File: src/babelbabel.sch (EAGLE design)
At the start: 86 parts, among them CON1 CON-4P-TABS-JST_GH-RA, CON10 CON-6P-SM06B, CON11 PINHEAD_1X04-2.54, CON12 PINHEAD_1X06-2.54, CON15 PINHEAD_1X04-2.54, CON16 CON-4P-TABS-JST_GH-RA, CON2 PINHEAD_1X04-2.54, CON3 PINHEAD_1X04-2.54, CON4 USB-AA-PTH, CON5 CON-4P-TABS-JST_GH-RA, CON6 CON-4P-TABS-JST_GH-RA, CON7 USB-1, IC1 NS5B1G385, IC13 STM32F103CBT7, IC14 74LVC2T45, IC15 74LVC2T45, IC16 74LVC2T45, IC17 74LVC2T45, IC2 NS5B1G385, IC3 AP2127-3.3, IC9 FE1.1S, J1 CONNECTION-SMD, J2 CONNECTION-SMD, Q7 8MHz, Q8 12MHz, Q9 NTZD3152PT1G

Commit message: Revert "source files consistency fix"
This reverts commit 015ba0159d9c48fa3345c98b8ff1ca9c9c6bfb7d.
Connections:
- new net ITDI: IC15.2A
- new net ITDO: IC16.1A
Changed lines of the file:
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@@
 </ports>
 <variantdefs>
-<variantdef name="48_pin_MCU"/>
-<variantdef name="64_pin_MCU"/>
+<variantdef name="A"/>
+<variantdef name="basic"/>
 </variantdefs>
 <parts>
 <part name="IC1" library="stm32" library_urn="urn:adsk.eagle:library:2473361" deviceset="STM32F373CBT6" device="-LQFP48" package3d_urn="urn:adsk.eagle:package:2473350/4">
-<variant name="64_pin_MCU" populate="no"/>
+<variant name="basic" populate="no"/>
 </part>
 <part name="GND1" library="supply_symbols" library_urn="urn:adsk.eagle:library:5017758" deviceset="GND" device="" value="GND"/>
@@
 <part name="P+6" library="supply_symbols" library_urn="urn:adsk.eagle:library:5017758" deviceset="3.3V" device=""/>
 <part name="GND4" library="supply_symbols" library_urn="urn:adsk.eagle:library:5017758" deviceset="GND" device="" value="GND"/>
-<part name="IC8" library="misc" library_urn="urn:adsk.eagle:library:5347860" deviceset="TPD3S014DBVR" device="-SOT23-6" package3d_urn="urn:adsk.eagle:package:1040217/3"/>
+<part name="IC8" library="misc" library_urn="urn:adsk.eagle:library:5347860" deviceset="TPD3S014DBVR" device="-SOT23-6" package3d_urn="urn:adsk.eagle:package:1040217/3">
+<variant name="A" populate="no"/>
+</part>
 <part name="+P4" library="supply_symbols" library_urn="urn:adsk.eagle:library:13097679" deviceset="5V" device=""/>
 <part name="C84" library="rc" library_urn="urn:adsk.eagle:library:2539423" deviceset="C" device="-0402" package3d_urn="urn:adsk.eagle:package:2539461/2" value="0.1uF">
@@
 <part name="IC2" library="stm32" library_urn="urn:adsk.eagle:library:2473361" deviceset="STM32F373RCT6" device="" package3d_urn="urn:adsk.eagle:package:2473349/4">
 <attribute name="DIGIKEY#" value="497-13252-ND"/>
-<variant name="48_pin_MCU" populate="no"/>
 </part>
 <part name="P+11" library="supply_symbols" library_urn="urn:adsk.eagle:library:5017758" deviceset="3.3V" device=""/>
@@
 <pinref part="IC1" gate="G$1" pin="BOOT0"/>
 <pinref part="R11" gate="G$1" pin="2"/>
-<label x="265.684" y="164.084" size="1.27" layer="95" rot="R90"/>
 </segment>
 <segment>
@@
 <part name="+P40" library="supply_symbols" library_urn="urn:adsk.eagle:library:5017758" deviceset="3.3V" device=""/>
 <part name="GND90" library="supply_symbols" library_urn="urn:adsk.eagle:library:5017758" deviceset="GND" device="" value="GND"/>
-<part name="CON11" library="pinhead" library_urn="urn:adsk.eagle:library:2540341" deviceset="PINHEAD_1X04" device="-2.54" package3d_urn="urn:adsk.eagle:package:2540383/2">
-<variant name="Electronic terminator" populate="no"/>
-<variant name="Mechanical terminator" populate="no"/>
-</part>
+<part name="CON11" library="pinhead" library_urn="urn:adsk.eagle:library:2540341" deviceset="PINHEAD_1X04" device="-2.54" package3d_urn="urn:adsk.eagle:package:2540383/2"/>
 <part name="CON12" library="pinhead" library_urn="urn:adsk.eagle:library:2540341" deviceset="PINHEAD_1X06" device="-2.54" package3d_urn="urn:adsk.eagle:package:2540381/2"/>
 <part name="GND91" library="supply_symbols" library_urn="urn:adsk.eagle:library:5017758" deviceset="GND" device="" value="GND"/>
@@
 </plain>
 <moduleinsts>
-<moduleinst name="BABEL1" module="BABEL" modulevariant="64_pin_MCU" x="190.5" y="134.62" offset="100">
+<moduleinst name="BABEL1" module="BABEL" modulevariant="basic" x="190.5" y="134.62" offset="100">
 <attribute name="NAME" x="190.5" y="145.796" size="2.032" layer="95" align="bottom-center"/>
 </moduleinst>
-<moduleinst name="BABEL2" module="BABEL" modulevariant="64_pin_MCU" x="190.5" y="60.96" offset="200">
+<moduleinst name="BABEL2" module="BABEL" modulevariant="basic" x="190.5" y="60.96" offset="200">
 <attribute name="NAME" x="190.5" y="72.136" size="2.032" layer="95" align="bottom-center"/>
 </moduleinst>
@@
 </segment>
 </net>
+<net name="ITDI" class="0">
+<segment>
+<pinref part="IC15" gate="G$1" pin="2A"/>
+<wire x1="203.2" y1="137.16" x2="200.66" y2="137.16" width="0.1524" layer="91"/>
+<label x="200.66" y="137.16" size="1.27" layer="95" rot="R180" xref="yes"/>
+</segment>
+</net>
 <net name="XTCK" class="0">
 <segment>
@@
 </segment>
 </net>
+<net name="ITDO" class="0">
+<segment>
+<pinref part="IC16" gate="G$1" pin="1A"/>
+<wire x1="203.2" y1="119.38" x2="200.66" y2="119.38" width="0.1524" layer="91"/>
+<label x="200.66" y="119.38" size="1.27" layer="95" rot="R180" xref="yes"/>
+</segment>
+</net>

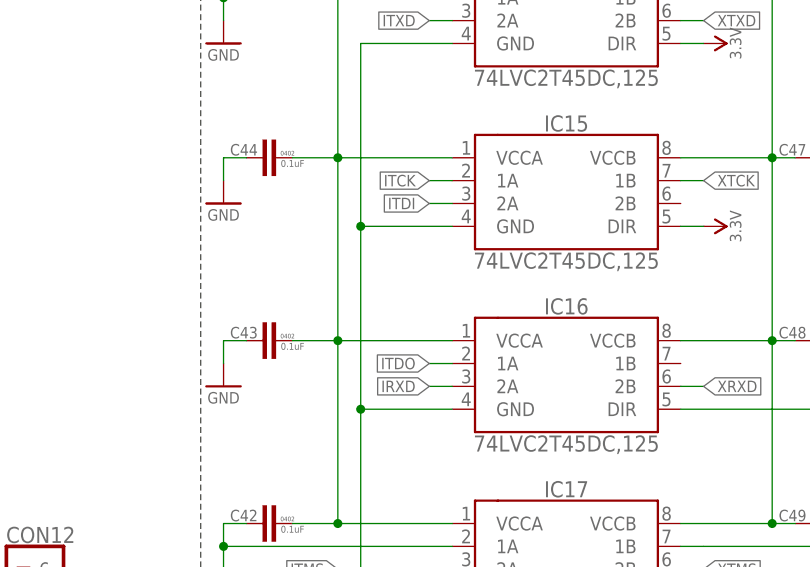
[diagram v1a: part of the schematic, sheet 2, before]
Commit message: source files consistency fix
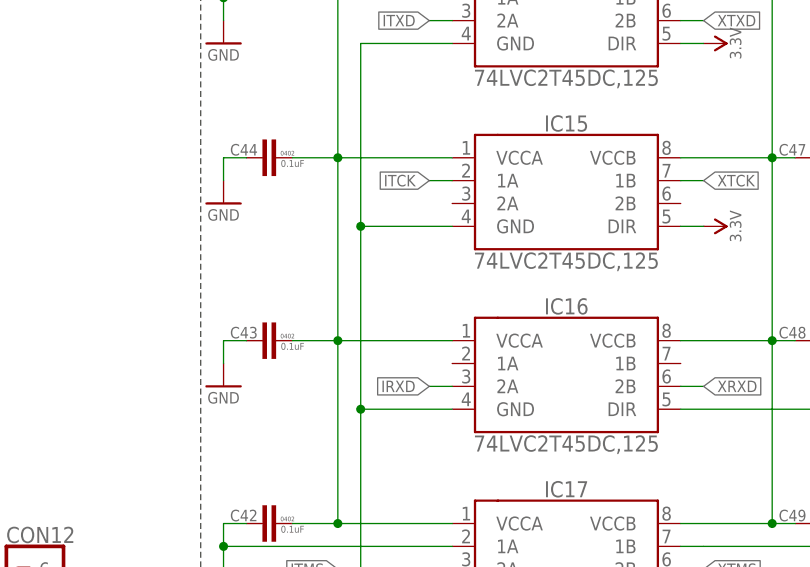
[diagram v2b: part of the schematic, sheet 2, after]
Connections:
- removed net ITDI: IC15.2A
- removed net ITDO: IC16.1A
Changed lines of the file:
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@@
 </ports>
 <variantdefs>
-<variantdef name="A"/>
-<variantdef name="basic"/>
+<variantdef name="48_pin_MCU"/>
+<variantdef name="64_pin_MCU"/>
 </variantdefs>
 <parts>
 <part name="IC1" library="stm32" library_urn="urn:adsk.eagle:library:2473361" deviceset="STM32F373CBT6" device="-LQFP48" package3d_urn="urn:adsk.eagle:package:2473350/4">
-<variant name="basic" populate="no"/>
+<variant name="64_pin_MCU" populate="no"/>
 </part>
 <part name="GND1" library="supply_symbols" library_urn="urn:adsk.eagle:library:5017758" deviceset="GND" device="" value="GND"/>
@@
 <part name="P+6" library="supply_symbols" library_urn="urn:adsk.eagle:library:5017758" deviceset="3.3V" device=""/>
 <part name="GND4" library="supply_symbols" library_urn="urn:adsk.eagle:library:5017758" deviceset="GND" device="" value="GND"/>
-<part name="IC8" library="misc" library_urn="urn:adsk.eagle:library:5347860" deviceset="TPD3S014DBVR" device="-SOT23-6" package3d_urn="urn:adsk.eagle:package:1040217/3">
-<variant name="A" populate="no"/>
-</part>
+<part name="IC8" library="misc" library_urn="urn:adsk.eagle:library:5347860" deviceset="TPD3S014DBVR" device="-SOT23-6" package3d_urn="urn:adsk.eagle:package:1040217/3"/>
 <part name="+P4" library="supply_symbols" library_urn="urn:adsk.eagle:library:13097679" deviceset="5V" device=""/>
 <part name="C84" library="rc" library_urn="urn:adsk.eagle:library:2539423" deviceset="C" device="-0402" package3d_urn="urn:adsk.eagle:package:2539461/2" value="0.1uF">
@@
 <part name="IC2" library="stm32" library_urn="urn:adsk.eagle:library:2473361" deviceset="STM32F373RCT6" device="" package3d_urn="urn:adsk.eagle:package:2473349/4">
 <attribute name="DIGIKEY#" value="497-13252-ND"/>
+<variant name="48_pin_MCU" populate="no"/>
 </part>
 <part name="P+11" library="supply_symbols" library_urn="urn:adsk.eagle:library:5017758" deviceset="3.3V" device=""/>
@@
 <pinref part="IC1" gate="G$1" pin="BOOT0"/>
 <pinref part="R11" gate="G$1" pin="2"/>
+<label x="265.684" y="164.084" size="1.27" layer="95" rot="R90"/>
 </segment>
 <segment>
@@
 <part name="+P40" library="supply_symbols" library_urn="urn:adsk.eagle:library:5017758" deviceset="3.3V" device=""/>
 <part name="GND90" library="supply_symbols" library_urn="urn:adsk.eagle:library:5017758" deviceset="GND" device="" value="GND"/>
-<part name="CON11" library="pinhead" library_urn="urn:adsk.eagle:library:2540341" deviceset="PINHEAD_1X04" device="-2.54" package3d_urn="urn:adsk.eagle:package:2540383/2"/>
+<part name="CON11" library="pinhead" library_urn="urn:adsk.eagle:library:2540341" deviceset="PINHEAD_1X04" device="-2.54" package3d_urn="urn:adsk.eagle:package:2540383/2">
+<variant name="Electronic terminator" populate="no"/>
+<variant name="Mechanical terminator" populate="no"/>
+</part>
 <part name="CON12" library="pinhead" library_urn="urn:adsk.eagle:library:2540341" deviceset="PINHEAD_1X06" device="-2.54" package3d_urn="urn:adsk.eagle:package:2540381/2"/>
 <part name="GND91" library="supply_symbols" library_urn="urn:adsk.eagle:library:5017758" deviceset="GND" device="" value="GND"/>
@@
 </plain>
 <moduleinsts>
-<moduleinst name="BABEL1" module="BABEL" modulevariant="basic" x="190.5" y="134.62" offset="100">
+<moduleinst name="BABEL1" module="BABEL" modulevariant="64_pin_MCU" x="190.5" y="134.62" offset="100">
 <attribute name="NAME" x="190.5" y="145.796" size="2.032" layer="95" align="bottom-center"/>
 </moduleinst>
-<moduleinst name="BABEL2" module="BABEL" modulevariant="basic" x="190.5" y="60.96" offset="200">
+<moduleinst name="BABEL2" module="BABEL" modulevariant="64_pin_MCU" x="190.5" y="60.96" offset="200">
 <attribute name="NAME" x="190.5" y="72.136" size="2.032" layer="95" align="bottom-center"/>
 </moduleinst>
@@
 </segment>
 </net>
-<net name="ITDI" class="0">
-<segment>
-<pinref part="IC15" gate="G$1" pin="2A"/>
-<wire x1="203.2" y1="137.16" x2="200.66" y2="137.16" width="0.1524" layer="91"/>
-<label x="200.66" y="137.16" size="1.27" layer="95" rot="R180" xref="yes"/>
-</segment>
-</net>
 <net name="XTCK" class="0">
 <segment>
@@
 </segment>
 </net>
-<net name="ITDO" class="0">
-<segment>
-<pinref part="IC16" gate="G$1" pin="1A"/>
-<wire x1="203.2" y1="119.38" x2="200.66" y2="119.38" width="0.1524" layer="91"/>
-<label x="200.66" y="119.38" size="1.27" layer="95" rot="R180" xref="yes"/>
-</segment>
-</net>

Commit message: Attribute updates for manufacturability (#4)
Co-authored-by: Alexander Sysoev <alexander.sysoev@zubax.com>
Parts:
- CON10: LCSC# (none) -> C160405
- CON4: LCSC# (none) -> C39437
- CON7: LCSC# (none) -> C132562
- IC1, IC2: LCSC# (none) -> C889718
- S1, S2, S3, S4: LCSC# (none) -> C319063; MANF (none) -> XKB Connectivity; MANF# (none) -> DS-01RP

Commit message: connected Vref to VDD, fixes #10
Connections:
- net VDD_3V3: now also IC2.VREF+
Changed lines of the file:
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@@
 <segment>
 <pinref part="IC2" gate="G$1" pin="VDD@1"/>
-<wire x1="129.54" y1="127" x2="129.54" y2="116.84" width="0.1524" layer="91"/>
 <pinref part="P+13" gate="G$1" pin="VDD_3V3"/>
+<wire x1="129.54" y1="127" x2="129.54" y2="119.38" width="0.1524" layer="91"/>
+<pinref part="IC2" gate="G$1" pin="VREF+"/>
+<wire x1="129.54" y1="119.38" x2="129.54" y2="116.84" width="0.1524" layer="91"/>
+<wire x1="124.46" y1="127" x2="124.46" y2="119.38" width="0.1524" layer="91"/>
+<wire x1="124.46" y1="119.38" x2="129.54" y2="119.38" width="0.1524" layer="91"/>
+<junction x="129.54" y="119.38"/>
 </segment>
 <segment>
